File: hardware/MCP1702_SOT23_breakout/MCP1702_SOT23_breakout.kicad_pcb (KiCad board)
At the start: 2 copper layers, 2 parts

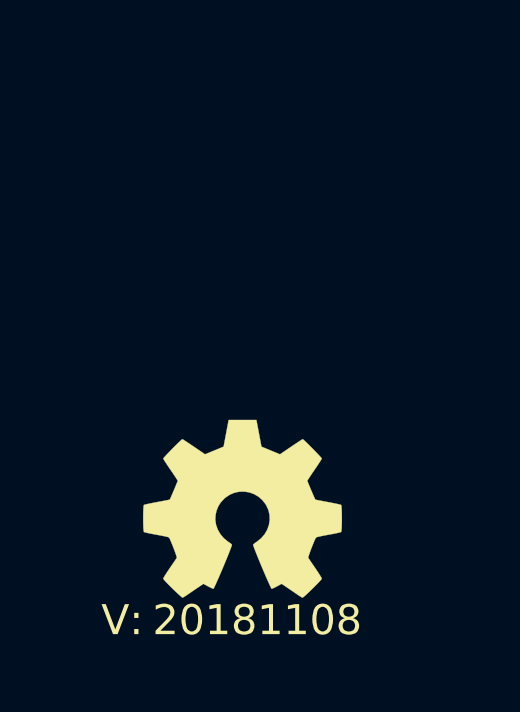
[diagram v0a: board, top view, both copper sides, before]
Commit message: layout done, now lets wait one day
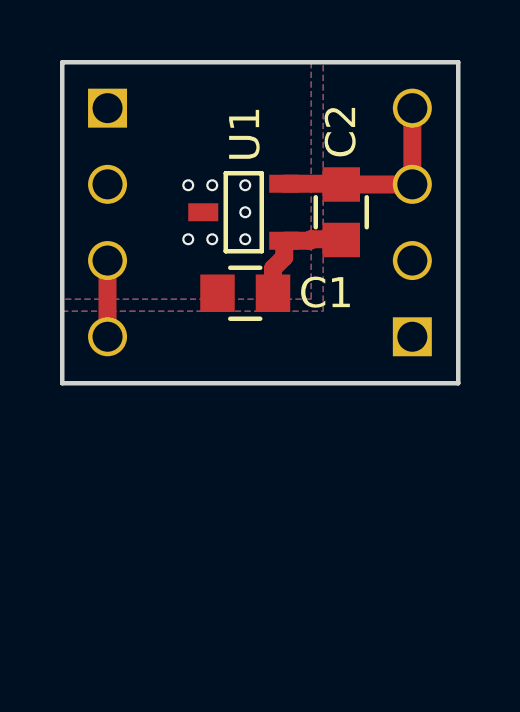
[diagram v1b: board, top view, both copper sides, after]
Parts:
- added C1: TBD, SquantorRcl:C_0805+0603, F.Cu at (148.1, 93.8)
- added C2: TBD, SquantorRcl:C_0805+0603, F.Cu at (151.3, 91.1)
- added J1: reference_input, SquantorConnectorsNamed:reference_input, B.Cu at (143.5, 91.4)
- added J2: reference_output, SquantorConnectorsNamed:reference_output, B.Cu at (153.7, 91.4)
- added U1: MCP1702-CB, SquantorIC:SOT23-3-Microchip-CB, F.Cu at (148.1, 91.1)
- N1: moved to B.Cu
- N2: value 20181108 -> 20190503
- moved N1 11.2 mm to (148.6, 89.8), turned to 180 degrees
- moved N2 9.11 mm to (149.3, 95.7)
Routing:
- net /VOUT: track 0.00 -> 6.87 mm
- net /VSS: track 0.00 -> 6.37 mm
- net /VIN: vias 0 -> 7
- added copper zone on B.Cu, net /VIN
- added copper zone on F.Cu, net /VIN
- added copper zone on B.Cu, net /VSS
- added copper zone on F.Cu, net /VSS
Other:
- board outline added: 13.2 x 10.7 mm

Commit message: final checks for SOT23 reference breakout, MCP1702 SOT23 breakout
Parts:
- N2: value 20190503 -> 20190505
- moved N2 0.40 mm to (149.3, 96.1)
- moved N1 0.20 mm to (148.6, 90.0)
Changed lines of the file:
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@@
   )
   (setup
-    (last_trace_width 0.6)
+    (last_trace_width 0.1524)
     (user_trace_width 0.1524)
     (user_trace_width 0.2)
@@
     (tags "PIN HEADER")
     (attr virtual)
-    (fp_text reference J2 (at -2.36 -3.47 90) (layer B.SilkS)
+    (fp_text reference J2 (at -2.06 -2.07 90) (layer B.SilkS)
       (effects (font (size 1 1) (thickness 0.15)) (justify mirror))
     )
@@
       (effects (font (size 0.6 0.6) (thickness 0.125)) (justify mirror))
     )
-    (fp_text user VSS (at -2.56 -1.97 180) (layer B.SilkS)
+    (fp_text user VSS (at -3.46 -2.37 180) (layer B.SilkS)
       (effects (font (size 0.6 0.6) (thickness 0.125)) (justify mirror))
     )
@@
     (tags "PIN HEADER")
     (attr virtual)
-    (fp_text reference J1 (at 2.46 -3.69 90) (layer B.SilkS)
+    (fp_text reference J1 (at 2.06 -2.19 90) (layer B.SilkS)
       (effects (font (size 1 1) (thickness 0.15)) (justify mirror))
     )
@@
       (effects (font (size 1 1) (thickness 0.15)) (justify mirror))
     )
-    (fp_text user VSS (at 2.56 -1.99) (layer B.SilkS)
+    (fp_text user VSS (at 3.46 -2.39) (layer B.SilkS)
       (effects (font (size 0.6 0.6) (thickness 0.125)) (justify mirror))
     )
-    (fp_text user VIN (at -4.44 -2.19 180) (layer B.SilkS)
+    (fp_text user VIN (at -4.44 -2.29 180) (layer B.SilkS)
       (effects (font (size 0.6 0.6) (thickness 0.125)) (justify mirror))
     )
@@
   )
   (module Symbols:OSHW-Symbol_6.7x6mm_SilkScreen (layer B.Cu)
-    (at 148.6 89.8 180)
+    (at 148.6 90 180)
     (descr "Open Source Hardware Symbol")
     (tags "Logo Symbol OSHW")
@@
   )
   (module SquantorLabels:Label_version (layer F.Cu)
-    (at 149.3 95.7)
+    (at 149.3 96.1)
     (fp_text reference N2 (at 0 1.4) (layer F.Fab) hide
       (effects (font (size 1 1) (thickness 0.15)))
     )
-    (fp_text value 20190503 (at -1.3 -0.1) (layer B.SilkS)
+    (fp_text value 20190505 (at -1.3 -0.1) (layer B.SilkS)
       (effects (font (size 0.8 0.8) (thickness 0.15)) (justify mirror))
     )
